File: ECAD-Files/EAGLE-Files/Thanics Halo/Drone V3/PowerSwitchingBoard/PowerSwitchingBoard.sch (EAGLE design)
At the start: 72 parts, among them IC1 MEGA8-AI, J1 ESC_CONTACTS, Q1 BC817, Q2 BC817, Q3 IRLR8726, Q4 IRLR8726, Q5 IRLR8726, Q6 IRLR8726, Q7 BC817, Q8 IRLR8726, Q9 IRLR8726, U1 TPS65261RHBR

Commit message: Added Flight ESCs and power supply to PowerSwitchingBoard
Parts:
- removed R12: 10k, 10k-resistor:ERA-6AEB103V
- added C10, C48, C6: 470uF, 470uF-capacitor:UWT1E471MNL1GSPCAP_10X10-ELECT-M
- added C11, C27, C45: 10nF, thanics_robotics:10NF_CAPACITOR
- added C12, C38, C46: 0.1uF, 0.1uF X7R Ceramic Capacitor:08055C104KAT2A
- added C26, C44, C47, C9: 10uF, 10uF X5R Ceramic Capacitor:GRM21BR60J106ME19L
- added C28, C29, C30, C33, C34, C35, C39, C40, C41: 0.1uF (50V), 0.1uF-capacitor-0402:0402ZD104KAT2A0402-M
- added C31, C36, C42, C5: 0.1uF, 0.1uF-capacitor-0402:0402ZD104KAT2A0402-M
- added C32, C37, C43, C7: 2.2uF, 2.2uF X5R Capacitor:GRM188R61C225KE15JG-188-M
- added C8: 22uF, 22uF X5R Ceramic Capacitor:GRM21BR60J226ME39L
- added D10, D11, D12, D13, D14, D15, D7, D8, D9: 1N4148, 1n4148w-diode:1N4148W-7-FSOD123-M
- added IC3, IC4, IC5: MEGA8-AI, atmel:MEGA8-AI
- added JP3, JP4, JP5: JUMPER-SMT_2_NO_NO-SILK, SparkFun-Jumpers:JUMPER-SMT_2_NO_NO-SILK
- added Q19, Q22, Q25, Q28, Q31, Q34, Q37, Q40, Q43: BC817, SparkFun-DiscreteSemi:TRANS_NPN-MMBTA42
- added Q20, Q21, Q23, Q24, Q26, Q27, Q29, Q30, Q32, Q33, Q35, Q36, Q38, Q39, Q41, Q42, Q44, Q45: IRLR8726, thanics_robotics:IRLR8726
- added R100, R105, R121, R127, R132, R67, R73, R78, R94: 2.2k, 2.2k-resistor:RC0603JR-072K2LRC0603N-M
- added R101, R106, R114, R115, R116, R122, R128, R133, R141, R142, R143, R68, R74, R79, R87, R88, R89, R95: 4.7k, 4.7k-resistor:RC0603JR-074K7LRC0603N-M
- added R102, R103, R107, R108, R124, R125, R129, R130, R134, R135, R70, R71, R75, R76, R80, R81, R97, R98: 100R, 100-resistor:RC0603JR-07100RLRC0603N-M
- added R104, R117, R118, R119, R120, R126, R131, R144, R145, R37, R38, R65, R66, R72, R77, R90, R91, R92, R93, R99: 10k, 10k-resistor(0603):RC0603JR-0710KLRC0603N-M
- added R109, R110, R111, R112, R113, R123, R136, R137, R138, R139, R140, R69, R82, R83, R84, R85, R86, R96: 47k, 47k-resistor:RC0603JR-0747KLRC0603N-M
- added U2, U3: SN74LS139ADRD16-M, sn74ls139:SN74LS139ADRD16-M
- added U4, U5, U6: DRV8313, DRV8313_BLDC_Driver:DRV8313PWPRPWP28_5P18X3P1-M
- added U7: 74LVC1G10DW-7, 3-input-nand:74LVC1G10DW-7
- added U8: STM32F103RCT6LQFP-64-M, stm32f103:STM32F103RCT6LQFP-64-M
- added X1, X3, X4, X5: 16MHz, thanics_robotics:CSTCE16
- C19: value 10uF -> 22uF; device thanics_robotics:10UF_CAPACITOR -> 22uF X5R Ceramic Capacitor:GRM21BR60J226ME39L
- C25: value 100uF -> 22uF; device thanics_robotics:100UF_CER_CAPACITOR -> 22uF X5R Ceramic Capacitor:GRM21BR60J226ME39L
- Q3: value IRLR8726 -> BC817; device thanics_robotics:IRLR8726 -> SparkFun-DiscreteSemi:TRANS_NPN-MMBTA42
- Q7: value BC817 -> IRLR8726; device SparkFun-DiscreteSemi:TRANS_NPN-MMBTA42 -> thanics_robotics:IRLR8726
- R10, R11: device 10k-resistor:ERA-6AEB103V -> 10k-resistor(0603):RC0603JR-0710KLRC0603N-M
- R2: value 100k -> 10k; device 100k-resistor:RC0603JR-07100KLRC0603N-M -> 10k-resistor(0603):RC0603JR-0710KLRC0603N-M
- R9: value 158k -> 20k; device 158k-resistor:RC0402FR-07150KLRC0402N-M -> 20k-resistor:RC0402FR-0720KLRC0402N-M
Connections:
- removed net +10V: C25.2, L1.1, R12.11, R9.11
- removed net N$46: IC1.PB3(MOSI/OC2)
- removed net N$48: IC1.PB5(SCK)
- removed net V_BATT: C13.2, C18.2, C2.2, U1.PVIN1, U1.PVIN2, U1.PVIN3, U1.VIN
- new net +1V8: C25.22, L1.1, R9.11
- new net A0: U4.IN1, U8.PB1
- new net A1: U5.IN1, U8.PA6
- new net A2: U6.IN1, U8.PB9
- new net AHIN2: IC4.PC4(ADC4/SDA), R95.22
- new net AHIN3: IC3.PC4(ADC4/SDA), R68.22
- new net AHIN4: IC5.PC4(ADC4/SDA), R122.22
- new net ALIN2: IC4.PD0(RXD), R92.11, R98.22
- new net ALIN3: IC3.PD0(RXD), R65.11, R71.22
- new net ALIN4: IC5.PD0(RXD), R119.11, R125.22
- new net AOUT2: C33.2, Q29.S, Q30.D, R113.11
- new net AOUT3: C28.2, Q20.S, Q21.D, R86.11
- new net AOUT4: C39.2, Q38.S, Q39.D, R140.11
- new net A_SENSE2: IC4.PC1(ADC1), R110.11, R113.22, R114.11
- new net A_SENSE3: IC3.PC1(ADC1), R83.11, R86.22, R87.11
- new net A_SENSE4: IC5.PC1(ADC1), R137.11, R140.22, R141.11
- new net B0: U4.IN2, U8.PB0
- new net B1: U5.IN2, U8.PA3
- new net B2: U6.IN2, U8.PA1
- new net BHIN2: IC4.PD1(TXD), R101.22
- new net BHIN3: IC3.PD1(TXD), R74.22
- new net BHIN4: IC5.PD1(TXD), R128.22
- new net BLIN2: IC4.PC5(ADC5/SCL), R103.22, R99.11
- new net BLIN3: IC3.PC5(ADC5/SCL), R72.11, R76.22
- new net BLIN4: IC5.PC5(ADC5/SCL), R126.11, R130.22
- new net BOOT1: U8.PB2
- new net BOUT2: C34.2, Q32.S, Q33.D, R112.11
- new net BOUT3: C29.2, Q23.S, Q24.D, R85.11
- new net BOUT4: C40.2, Q41.S, Q42.D, R139.11
- new net B_SENSE2: IC4.PC0(ADC0), R109.11, R112.22, R115.11
- new net B_SENSE3: IC3.PC0(ADC0), R82.11, R85.22, R88.11
- new net B_SENSE4: IC5.PC0(ADC0), R136.11, R139.22, R142.11
- new net C0: U4.IN3, U8.PA7
- new net C1: U5.IN3, U8.PA2
- new net C2: U6.IN3, U8.PB8
- new net CHIN2: IC4.PD3(INT1), R106.22
- new net CHIN3: IC3.PD3(INT1), R79.22
- new net CHIN4: IC5.PD3(INT1), R133.22
- new net CLIN2: IC4.PD5(T1), R104.11, R108.22
- new net CLIN3: IC3.PD5(T1), R77.11, R81.22
- new net CLIN4: IC5.PD5(T1), R131.11, R135.22
- new net COUT2: C35.2, Q35.S, Q36.D, R111.11
- new net COUT3: C30.2, Q26.S, Q27.D, R84.11
- new net COUT4: C41.2, Q44.S, Q45.D, R138.11
- new net C_SENSE2: IC4.ADC7, R111.22, R116.11, R96.11
- new net C_SENSE3: IC3.ADC7, R69.11, R84.22, R89.11
- new net C_SENSE4: IC5.ADC7, R123.11, R138.22, R143.11
- new net FAULT: U7.Y
- new net FAULT1: U4.!FAULT, U7.A
- new net FAULT2: U5.!FAULT, U7.B
- new net FAULT3: U6.!FAULT, U7.C
- new net LIPO: U8.PA5
- new net MISO: U3.!2G
- new net MISO1: IC1.PB4(MISO), U3.2Y0
- new net MISO2: IC4.PB4(MISO), U3.2Y1
- new net MISO3: IC3.PB4(MISO), U3.2Y2
- new net MISO4: IC5.PB4(MISO), U3.2Y3
- new net MOSI: U3.!1G
- new net MOSI1: IC1.PB3(MOSI/OC2), U3.1Y0
- new net MOSI2: IC4.PB3(MOSI/OC2), U3.1Y1
- new net MOSI3: IC3.PB3(MOSI/OC2), U3.1Y2
- new net MOSI4: IC5.PB3(MOSI/OC2), U3.1Y3
- new net MOT0_1: U4.OUT1
- new net MOT0_2: U4.OUT2
- new net MOT0_3: U4.OUT3
- new net MOT1_1: U5.OUT1
- new net MOT1_2: U5.OUT2
- new net MOT1_3: U5.OUT3
- new net MOT2_1: U6.OUT1
- new net MOT2_2: U6.OUT2
- new net MOT2_3: U6.OUT3
- new net N$100: IC4.PB6(XTAL1/TOSC1), X4.2
- new net N$101: IC4.PB7(XTAL2/TOSC2), X4.1
- new net N$103: Q37.B, R122.11
- new net N$104: Q38.G, R124.11
- new net N$105: Q37.C, R121.22, R124.22
- new net N$106: C39.1, D13.12, R121.11
- new net N$107: Q39.G, R125.11
- new net N$108: Q40.B, R128.11
- new net N$109: Q41.G, R129.11
- new net N$110: Q40.C, R127.22, R129.22
- new net N$111: C40.1, D14.12, R127.11
- new net N$112: Q42.G, R130.11
- new net N$113: Q43.B, R133.11
- new net N$114: Q44.G, R134.11
- new net N$115: Q43.C, R132.22, R134.22
- new net N$116: C41.1, D15.12, R132.11
- new net N$117: Q45.G, R135.11
- new net N$118: IC5.PB0(ICP), R144.22
- new net N$119: IC5.ADC6, JP5.1
- new net N$120: C42.2, IC5.AREF
- new net N$121: IC5.PB6(XTAL1/TOSC1), X5.2
- new net N$122: IC5.PB7(XTAL2/TOSC2), X5.1
- new net N$44: IC1.PB0(ICP), R37.22
- new net N$61: Q19.B, R68.11
- new net N$62: Q20.G, R70.11
- new net N$63: Q19.C, R67.22, R70.22
- new net N$64: C28.1, D7.12, R67.11
- new net N$65: Q21.G, R71.11
- new net N$66: Q22.B, R74.11
- new net N$67: Q23.G, R75.11
- new net N$68: Q22.C, R73.22, R75.22
- new net N$69: C29.1, D8.12, R73.11
- new net N$70: Q24.G, R76.11
- new net N$71: Q25.B, R79.11
- new net N$72: Q26.G, R80.11
- new net N$73: Q25.C, R78.22, R80.22
- new net N$74: C30.1, D9.12, R78.11
- new net N$75: Q27.G, R81.11
- new net N$76: IC3.PB0(ICP), R90.22
- new net N$77: IC3.ADC6, JP3.1
- new net N$78: C31.2, IC3.AREF
- new net N$79: IC3.PB6(XTAL1/TOSC1), X3.2
- new net N$80: IC3.PB7(XTAL2/TOSC2), X3.1
- new net N$82: Q28.B, R95.11
- new net N$83: Q29.G, R97.11
- new net N$84: Q28.C, R94.22, R97.22
- new net N$85: C33.1, D10.12, R94.11
- new net N$86: Q30.G, R98.11
- new net N$87: Q31.B, R101.11
- new net N$88: Q32.G, R102.11
- new net N$89: Q31.C, R100.22, R102.22
- new net N$90: C34.1, D11.12, R100.11
- new net N$91: Q33.G, R103.11
- new net N$92: Q34.B, R106.11
- new net N$93: Q35.G, R107.11
- new net N$94: Q34.C, R105.22, R107.22
- new net N$95: C35.1, D12.12, R105.11
- new net N$96: Q36.G, R108.11
- new net N$97: IC4.PB0(ICP), R117.22
- new net N$98: IC4.ADC6, JP4.1
- new net N$99: C36.2, IC4.AREF
- new net NEUTRAL_SENSE2: IC4.PD6(AIN0), R109.22, R110.22, R96.22
- new net NEUTRAL_SENSE3: IC3.PD6(AIN0), R69.22, R82.22, R83.22
- new net NEUTRAL_SENSE4: IC5.PD6(AIN0), R123.22, R136.22, R137.22
- new net PW4: R144.11, R145.11
- new net PWM: R37.11, R38.11
- new net PWM2: R117.11, R118.11
- new net PWM3: R90.11, R91.11
- new net RESET: U8.NRST
- new net RST: U2.!1G
- new net RST1: IC1.PC6(/RESET), R3.11, U2.1Y0
- new net RST2: IC4.PC6(/RESET), R93.11, U2.1Y1
- new net RST3: IC3.PC6(/RESET), R66.11, U2.1Y2
- new net RST4: IC5.PC6(/RESET), R120.11, U2.1Y3
- new net SCK: U2.!2G
- new net SCK1: IC1.PB5(SCK), U2.2Y0
- new net SCK2: IC4.PB5(SCK), U2.2Y1
- new net SCK3: IC3.PB5(SCK), U2.2Y2
- new net SCK4: IC5.PB5(SCK), U2.2Y3
- new net SCL: U8.PB10
- new net SCL2: U8.PB6
- new net SDA: U8.PB11
- new net SDA2: U8.PB7
- new net SEL1: U2.1A, U2.2A, U3.1A, U3.2A
- new net SEL2: U2.1B, U2.2B, U3.1B, U3.2B
- new net SWCLK: U8.PA14
- new net SWDIO: U8.PA13
- net +3V3: now also C19.22, U8.VBAT, U8.VDDA, U8.VDD_1, U8.VDD_2, U8.VDD_3, U8.VDD_4; no longer C19.2, R10.11
- net +5V: now also C32.22, C37.22, C43.22, C7.22, IC3.AVCC, IC3.VCC@1, IC3.VCC@2, IC4.AVCC, IC4.VCC@1, IC4.VCC@2, IC5.AVCC, IC5.VCC@1, IC5.VCC@2, R120.22, R66.22, R93.22, U2.VCC, U3.VCC, U4.!RESET, U4.!SLEEP, U4.EN1, U4.EN2, U4.EN3, U5.!RESET, U5.!SLEEP, U5.EN1, U5.EN2, U5.EN3, U6.!RESET, U6.!SLEEP, U6.EN1, U6.EN2, U6.EN3, U7.VCC; no longer R11.11
- net AHIN: now also IC1.PC4(ADC4/SDA)
- net ALIN: now also IC1.PD0(RXD)
- net A_SENSE: now also IC1.PC1(ADC1)
- net BHIN: now also IC1.PD1(TXD)
- net BLIN: now also IC1.PC5(ADC5/SCL)
- net BOUT: now also Q6.S, Q7.D; no longer Q3.S, Q6.D
- net B_SENSE: now also IC1.PC0(ADC0)
- net CHIN: now also IC1.PD3(INT1)
- net CLIN: now also IC1.PD5(T1)
- net C_SENSE: now also IC1.ADC7
- net GND: now also C10.22, C19.11, C25.11, C26.11, C31.1, C32.11, C36.1, C37.11, C42.1, C43.11, C44.11, C47.11, C48.22, C5.1, C6.22, C7.11, C8.22, C9.22, IC1.GND, IC3.GND, IC3.GND@1, IC3.GND@2, IC4.GND, IC4.GND@1, IC4.GND@2, IC5.GND, IC5.GND@1, IC5.GND@2, JP1.2, JP3.2, JP4.2, JP5.2, Q19.E, Q21.S, Q22.E, Q24.S, Q25.E, Q27.S, Q28.E, Q3.E, Q30.S, Q31.E, Q33.S, Q34.E, Q36.S, Q37.E, Q39.S, Q40.E, Q42.S, Q43.E, Q45.S, Q7.S, R104.22, R114.22, R115.22, R116.22, R118.22, R119.22, R126.22, R131.22, R141.22, R142.22, R143.22, R145.22, R2.22, R38.22, R65.22, R72.22, R77.22, R87.22, R88.22, R89.22, R91.22, R92.22, R99.22, U2.GND, U3.GND, U4.EPAD, U4.GND, U4.GND_2, U4.GND_3, U4.PGND1, U4.PGND2, U4.PGND3, U5.EPAD, U5.GND, U5.GND_2, U5.GND_3, U5.PGND1, U5.PGND2, U5.PGND3, U6.EPAD, U6.GND, U6.GND_2, U6.GND_3, U6.PGND1, U6.PGND2, U6.PGND3, U7.GND, U8.VSSA, U8.VSS_1, U8.VSS_2, U8.VSS_3, U8.VSS_4, X1.GND, X3.GND, X4.GND, X5.GND; no longer C19.1, C25.1, Q6.S, Q7.E, R12.22
- net N$1: now also C11.1, U4.CPH; no longer IC1.PC6(/RESET), R3.11
- net N$10: now also Q6.G; no longer Q3.G
- net N$13: now also R2.11
- net N$17: now also R10.11
- net N$24: now also Q7.G; no longer Q6.G
- net N$25: now also Q3.B; no longer Q7.B
- net N$3: now also R11.11
- net N$31: now also Q3.C; no longer Q7.C
- net N$34: now also C5.2, IC1.AREF; no longer IC1.PC0(ADC0)
- net N$35: now also IC1.PB6(XTAL1/TOSC1), X1.2; no longer IC1.PC1(ADC1)
- net N$36: now also IC1.PB7(XTAL2/TOSC2), X1.1; no longer IC1.PC4(ADC4/SDA)
- net N$37: now also C11.2, U4.CPL; no longer IC1.PC5(ADC5/SCL)
- net N$38: now also JP1.1
- net N$39: now also C27.1, U5.CPH; no longer IC1.ADC7
- net N$40: now also C27.2, U5.CPL; no longer IC1.PD0(RXD)
- net N$41: now also C38.2, U5.VCP; no longer IC1.PD1(TXD)
- net N$42: now also C45.1, U6.CPH; no longer IC1.PD3(INT1)
- net N$43: now also C45.2, U6.CPL; no longer IC1.PD5(T1)
- net N$45: now also C46.2, U6.VCP; no longer IC1.PB0(ICP)
- net N$47: now also C12.2, U4.VCP; no longer IC1.PB4(MISO)
- net VDD: now also C10.11, C12.1, C13.2, C18.2, C2.2, C26.22, C38.1, C44.22, C46.1, C47.22, C48.11, C6.11, C8.11, C9.11, D10.21, D11.21, D12.21, D13.21, D14.21, D15.21, D7.21, D8.21, D9.21, Q20.D, Q23.D, Q26.D, Q29.D, Q32.D, Q35.D, Q38.D, Q41.D, Q44.D, Q6.D, U1.PVIN1, U1.PVIN2, U1.PVIN3, U1.VIN, U4.VM, U4.VM_2, U5.VM, U5.VM_2, U6.VM, U6.VM_2; no longer Q3.D
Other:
- note added: "Triple Buck Converter -5V -3V3 -1V8 **18V MAX INPUT (3-4S LiPo ONLY)**"
- note removed: "Triple Buck Converter -5V -3V3 -1V8 **17V MAX INPUT (3-4S LiPo ONLY)**"
- moved on the sheet: C1, C20, C21, C3, C4, D1, D2, D3, IC1, JP1, L1, Q1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

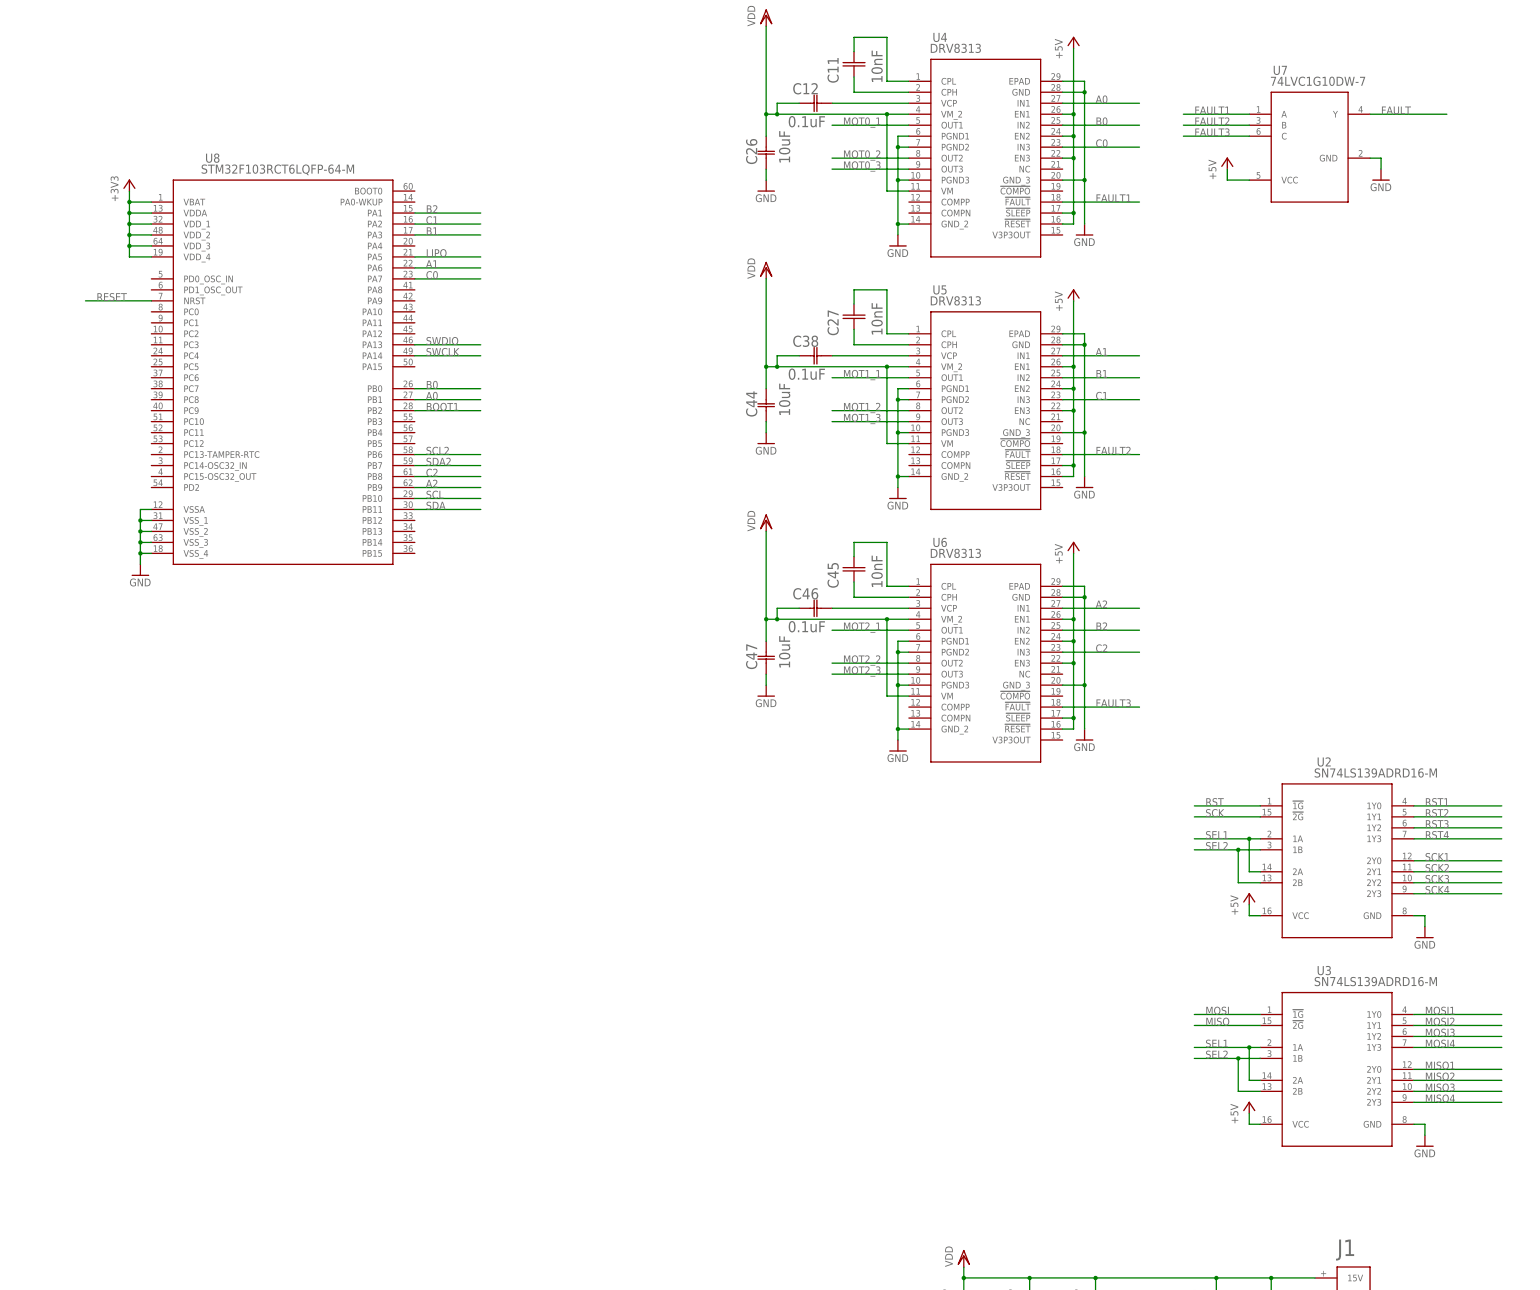
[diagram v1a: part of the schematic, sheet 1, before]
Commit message: Added connectors
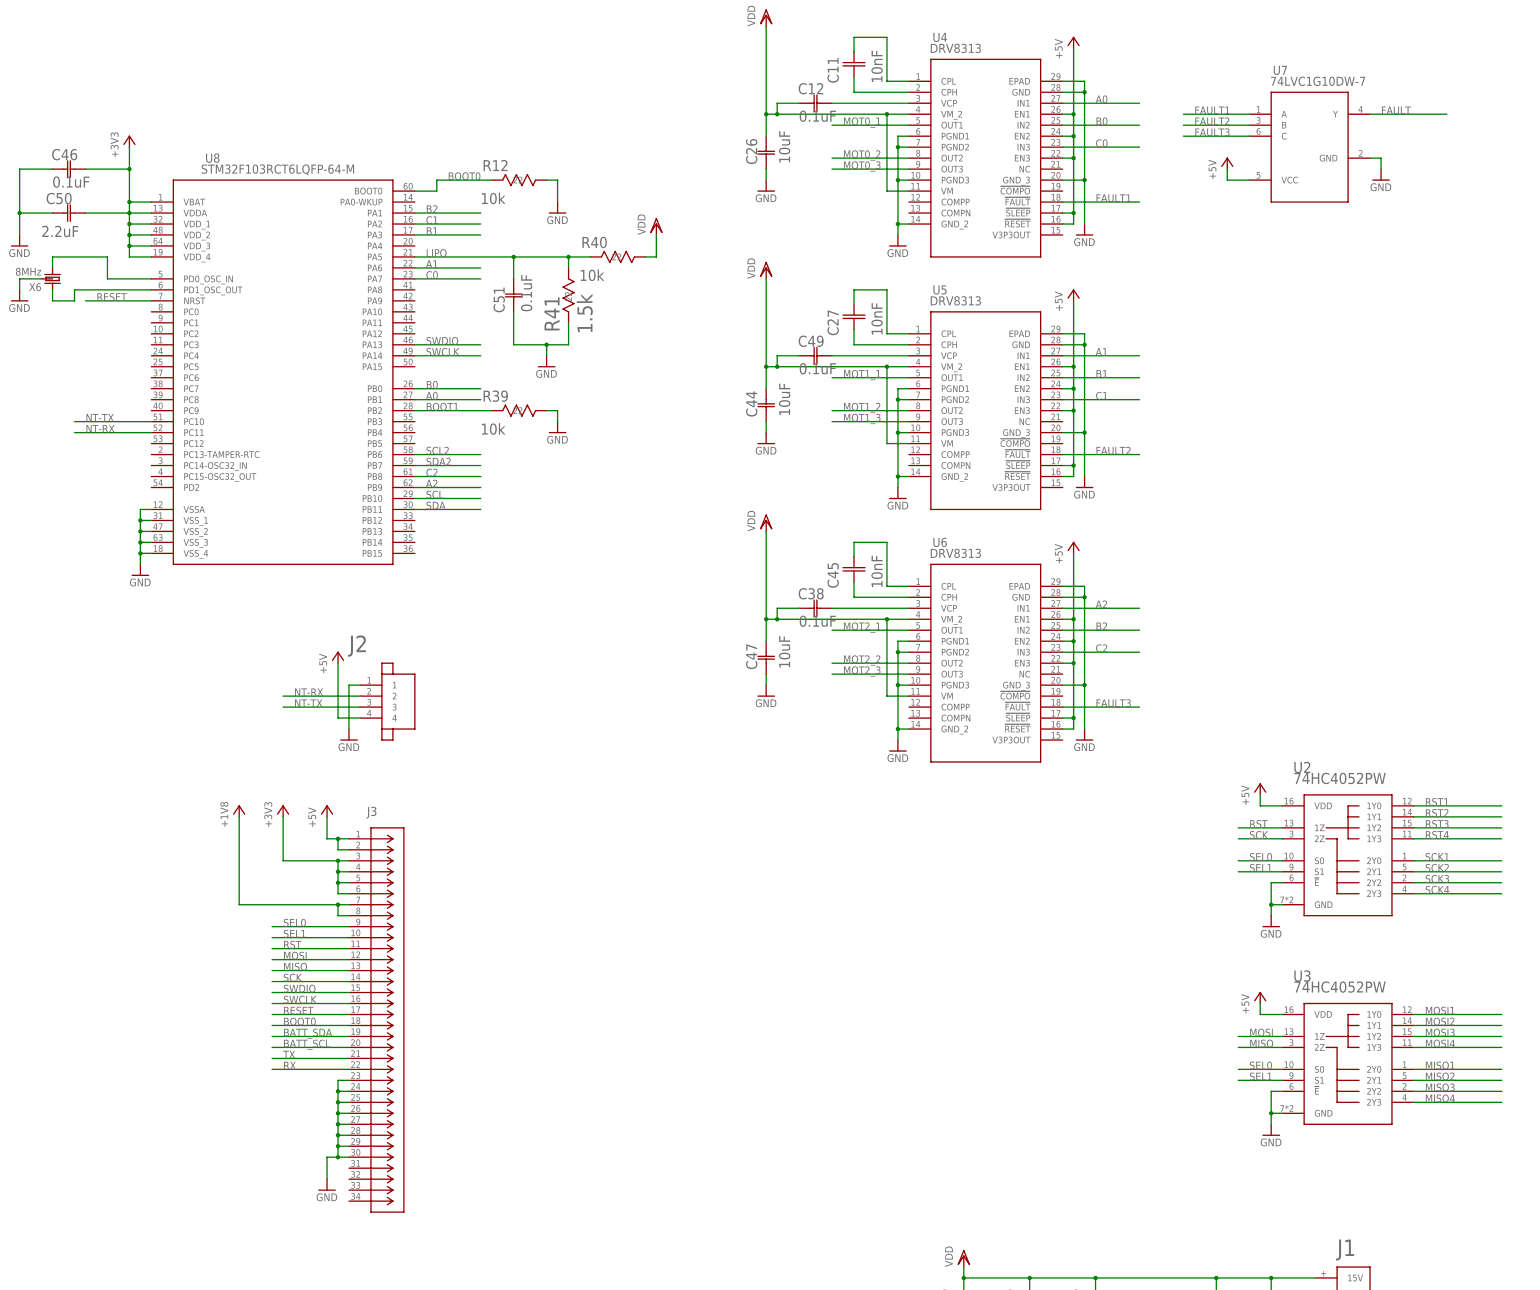
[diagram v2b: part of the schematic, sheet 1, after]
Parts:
- added C49, C51: 0.1uF, 0.1uF-capacitor-0402:0402ZD104KAT2A0402-M
- added C50: 2.2uF, 2.2uF X5R Capacitor:GRM188R61C225KE15JG-188-M
- added J2: (no value), thanics_robotics:JST_SH_4POS
- added J3: 62674-301121ALF, 30pin_ffc_connector:62674-301121ALF
- added R12, R39, R40: 10k, 10k-resistor(0603):RC0603JR-0710KLRC0603N-M
- added R41: 1.5k, 1.5k-resistor:RC0603JR-071K5LRC0603N-M
- added X6: 8MHz, thanics_robotics:CSTCE8M00G55Z
- C12, C38, C46: device 0.1uF X7R Ceramic Capacitor:08055C104KAT2A -> 0.1uF-capacitor-0402:0402ZD104KAT2A0402-M
- U2, U3: value SN74LS139ADRD16-M -> 74HC4052PW; device sn74ls139:SN74LS139ADRD16-M -> thanics_robotics:74HC4052PW
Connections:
- removed net SEL2: U2.1B, U2.2B, U3.1B, U3.2B
- new net BATT_SCL: J3.2020
- new net BATT_SDA: J3.1919
- new net BOOT0: J3.1818, R12.22, U8.BOOT0
- new net N$46: U8.PD0_OSC_IN, X6.2
- new net N$48: U8.PD1_OSC_OUT, X6.1
- new net NT-RX: J2.2, U8.PC11
- new net NT-TX: J2.3, U8.PC10
- new net RX: J3.2222
- new net SEL0: J3.99, U2.S0, U3.S0
- new net TX: J3.2121
- net +1V8: now also J3.77, J3.88
- net +3V3: now also C46.2, C50.22, J3.33, J3.44, J3.55, J3.66
- net +5V: now also J2.4, J3.11, J3.22, U2.VDD, U3.VDD; no longer U2.VCC, U3.VCC
- net BOOT1: now also R39.22
- net GND: now also C46.1, C50.11, C51.1, J2.1, J3.2323, J3.2424, J3.2525, J3.2626, J3.2727, J3.2828, J3.2929, J3.3030, R12.11, R39.11, R41.22, U2.!E, U3.!E, X6.GND
- net LIPO: now also C51.2, R40.22, R41.11
- net MISO: now also J3.1313, U3.2Z; no longer U3.!2G
- net MOSI: now also J3.1212, U3.1Z; no longer U3.!1G
- net N$41: now also C49.2; no longer C38.2
- net N$45: now also C38.2; no longer C46.2
- net RESET: now also J3.1717
- net RST: now also J3.1111, U2.1Z; no longer U2.!1G
- net SCK: now also J3.1414, U2.2Z; no longer U2.!2G
- net SEL1: now also J3.1010, U2.S1, U3.S1; no longer U2.1A, U2.2A, U3.1A, U3.2A
- net SWCLK: now also J3.1616
- net SWDIO: now also J3.1515
- net VDD: now also C49.1, R40.11; no longer C46.1
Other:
- moved on the sheet: C38, C46

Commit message: Fixed consistancy errors and finished routing
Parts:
- removed D13, D14, D15: 1N4148, 1n4148w-diode:1N4148W-7-FSOD123-M
- removed IC1: MEGA8-AI, atmel:MEGA8-AI
- removed R39: 10k, 10k-resistor(0603):RC0603JR-0710KLRC0603N-M
- added D4, D5, D6: 1N4148, 1n4148w-diode:1N4148W-7-FSOD123-M
- added GND, SCL, SDA: TPTP20SQ, testpad:TPTP20SQ
- added J4, J5, J6: B3B-ZR-SM4, jst:B3B-ZR-SM4
- Q1, Q19, Q2, Q22, Q25, Q28, Q3, Q31, Q34, Q37, Q40, Q43: value BC817 -> 500mA/300V
- U7: value 74LVC1G10DW-7 -> STM32F103RCT6LQFP-64-M; device 3-input-nand:74LVC1G10DW-7 -> stm32f103:STM32F103RCT6LQFP-64-M
- U8: value STM32F103RCT6LQFP-64-M -> MEGA8-AI; device stm32f103:STM32F103RCT6LQFP-64-M -> atmel:MEGA8-AI
- X6: device thanics_robotics:CSTCE8M00G55Z -> thanics_robotics:CSTCE8M00G55
- renumbered IC3 to U10, IC4 to U9, IC5 to U11
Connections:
- removed net BOOT1: R39.22, U8.PB2
- removed net PW4: R144.11, R145.11
- new net PWM4: J3.2626, R144.11, R145.11
- net +3V3: now also U7.VBAT, U7.VDDA, U7.VDD_1, U7.VDD_2, U7.VDD_3, U7.VDD_4; no longer U8.VBAT, U8.VDDA, U8.VDD_1, U8.VDD_2, U8.VDD_3, U8.VDD_4
- net +5V: now also U8.AVCC, U8.VCC@1, U8.VCC@2; no longer IC1.AVCC, IC1.VCC@1, IC1.VCC@2, U7.VCC
- net A0: now also U7.PB1; no longer U8.PB1
- net A1: now also U7.PA6; no longer U8.PA6
- net A2: now also U7.PB9; no longer U8.PB9
- net AHIN: now also U8.PC4(ADC4/SDA); no longer IC1.PC4(ADC4/SDA)
- net ALIN: now also U8.PD0(RXD); no longer IC1.PD0(RXD)
- net A_SENSE: now also U8.PC1(ADC1); no longer IC1.PC1(ADC1)
- net B0: now also U7.PB0; no longer U8.PB0
- net B1: now also U7.PA3; no longer U8.PA3
- net B2: now also U7.PA1; no longer U8.PA1
- net BATT_SCL: now also SCL.TP
- net BATT_SDA: now also SDA.TP
- net BHIN: now also U8.PD1(TXD); no longer IC1.PD1(TXD)
- net BLIN: now also U8.PC5(ADC5/SCL); no longer IC1.PC5(ADC5/SCL)
- net BOOT0: now also U7.BOOT0; no longer U8.BOOT0
- net B_SENSE: now also U8.PC0(ADC0); no longer IC1.PC0(ADC0)
- net C0: now also U7.PA7; no longer U8.PA7
- net C1: now also U7.PA2; no longer U8.PA2
- net C2: now also U7.PB8; no longer U8.PB8
- net CHIN: now also U8.PD3(INT1); no longer IC1.PD3(INT1)
- net CLIN: now also U8.PD5(T1); no longer IC1.PD5(T1)
- net C_SENSE: now also U8.ADC7; no longer IC1.ADC7
- net FAULT: now also J3.2727; no longer U7.Y
- net FAULT1: no longer U7.A
- net FAULT2: no longer U7.B
- net FAULT3: no longer U7.C
- net GND: now also GND.TP, U7.PB2, U7.VSSA, U7.VSS_1, U7.VSS_2, U7.VSS_3, U7.VSS_4, U8.GND, U8.GND@1, U8.GND@2; no longer IC1.GND, IC1.GND@1, IC1.GND@2, J3.2323, J3.2424, J3.2525, J3.2626, J3.2727, R39.11, U7.GND, U8.VSSA, U8.VSS_1, U8.VSS_2, U8.VSS_3, U8.VSS_4
- net LIPO: now also U7.PA5; no longer U8.PA5
- net MISO1: now also U8.PB4(MISO); no longer IC1.PB4(MISO)
- net MOSI1: now also U8.PB3(MOSI/OC2); no longer IC1.PB3(MOSI/OC2)
- net MOT0_1: now also J4.1
- net MOT0_2: now also J4.2
- net MOT0_3: now also J4.3
- net MOT1_1: now also J5.1
- net MOT1_2: now also J5.2
- net MOT1_3: now also J5.3
- net MOT2_1: now also J6.1
- net MOT2_2: now also J6.2
- net MOT2_3: now also J6.3
- net N$106: now also D10.12; no longer D13.12
- net N$111: now also D11.12; no longer D14.12
- net N$116: now also D12.12; no longer D15.12
- net N$34: now also U8.AREF; no longer IC1.AREF
- net N$35: now also U8.PB6(XTAL1/TOSC1); no longer IC1.PB6(XTAL1/TOSC1)
- net N$36: now also U8.PB7(XTAL2/TOSC2); no longer IC1.PB7(XTAL2/TOSC2)
- net N$38: now also U8.ADC6; no longer IC1.ADC6
- net N$44: now also U8.PB0(ICP); no longer IC1.PB0(ICP)
- net N$46: now also U7.PD0_OSC_IN; no longer U8.PD0_OSC_IN
- net N$48: now also U7.PD1_OSC_OUT; no longer U8.PD1_OSC_OUT
- net N$85: now also D4.12; no longer D10.12
- net N$90: now also D5.12; no longer D11.12
- net N$95: now also D6.12; no longer D12.12
- net NEUTRAL_SENSE: now also U8.PD6(AIN0); no longer IC1.PD6(AIN0)
- net NT-RX: now also U7.PC11; no longer U8.PC11
- net NT-TX: now also U7.PC10; no longer U8.PC10
- net PWM: now also J3.2323
- net PWM2: now also J3.2424
- net PWM3: now also J3.2525
- net RESET: now also U7.NRST; no longer U8.NRST
- net RST1: now also U8.PC6(/RESET); no longer IC1.PC6(/RESET)
- net RX: now also U7.PA10
- net SCK1: now also U8.PB5(SCK); no longer IC1.PB5(SCK)
- net SCL: now also U7.PB10; no longer U8.PB10
- net SCL2: now also U7.PB6; no longer U8.PB6
- net SDA: now also U7.PB11; no longer U8.PB11
- net SDA2: now also U7.PB7; no longer U8.PB7
- net SWCLK: now also U7.PA14; no longer U8.PA14
- net SWDIO: now also U7.PA13; no longer U8.PA13
- net TX: now also U7.PA9
- net VDD: now also D4.21, D5.21, D6.21; no longer D13.21, D14.21, D15.21
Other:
- moved on the sheet: D10, D11, D12

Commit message: Finished Power Switching Board and Flight Controller Board v1
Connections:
- removed net FAULT: J3.2727
- net GND: now also J3.2727
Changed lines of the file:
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@@
 <?xml version="1.0" encoding="utf-8"?>
 <!DOCTYPE eagle SYSTEM "eagle.dtd">
-<eagle version="8.7.0">
+<eagle version="8.7.1">
 <drawing>
 <settings>
@@
 <layers>
 <layer number="1" name="Top" color="4" fill="1" visible="no" active="no"/>
+<layer number="2" name="Route2" color="1" fill="3" visible="no" active="no"/>
+<layer number="15" name="Route15" color="4" fill="6" visible="no" active="no"/>
 <layer number="16" name="Bottom" color="1" fill="1" visible="no" active="no"/>
 <layer number="17" name="Pads" color="2" fill="1" visible="no" active="no"/>
@@
 <wire x1="-406.4" y1="55.88" x2="-406.4" y2="53.34" width="0.1524" layer="91"/>
 <junction x="-406.4" y="53.34"/>
+<pinref part="J3" gate="A" pin="2727"/>
+<wire x1="-403.86" y1="58.42" x2="-406.4" y2="58.42" width="0.1524" layer="91"/>
+<wire x1="-406.4" y1="58.42" x2="-406.4" y2="55.88" width="0.1524" layer="91"/>
+<junction x="-406.4" y="55.88"/>
 </segment>
 <segment>
@@
 </segment>
 </net>
-<net name="FAULT" class="0">
-<segment>
-<pinref part="J3" gate="A" pin="2727"/>
-<wire x1="-403.86" y1="58.42" x2="-421.64" y2="58.42" width="0.1524" layer="91"/>
-<label x="-419.1" y="58.42" size="1.778" layer="95"/>
-</segment>
-</net>

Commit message: Changed ethernet capacitor isolation to transformers
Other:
- note added: "ESC1"
- note added: "ESC2"
- note added: "ESC3"
- note added: "ESC4"
- note added: "Gimbal Control"
